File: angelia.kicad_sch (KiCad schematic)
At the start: 428 parts, among them J10 Conn_Coaxial, J15 Conn_02x05_Top_Bottom, J16 Conn_02x13_Top_Bottom, J18 Conn_02x05_Top_Bottom, J25 Conn_Coaxial, J3 Conn_Coaxial, J33 ATX-20, J5 Conn_Coaxial, J7 RJ45, P1 Conn_02x05_Top_Bottom, P2 Conn_02x05_Top_Bottom, P3 EP4CE115F780, U10 LTC2208xUP, U11 LTC6400, U13 KSZ9021RL, U14 SN65LVDM180D, U18 LTC2208xUP, U19 TO-252-5, U2 TLV320AIC23BPW, U20 74LCX541MTC, U22 ULN2003A, U23 LTC6400, U25 74LCX541MTC, U27 TO-252-3, U3 LMC6482AM, U31 TO-252-5, U4 LMC6482AM, U5 AD9744, U6 OPA2674IC, U7 OPA2674IC

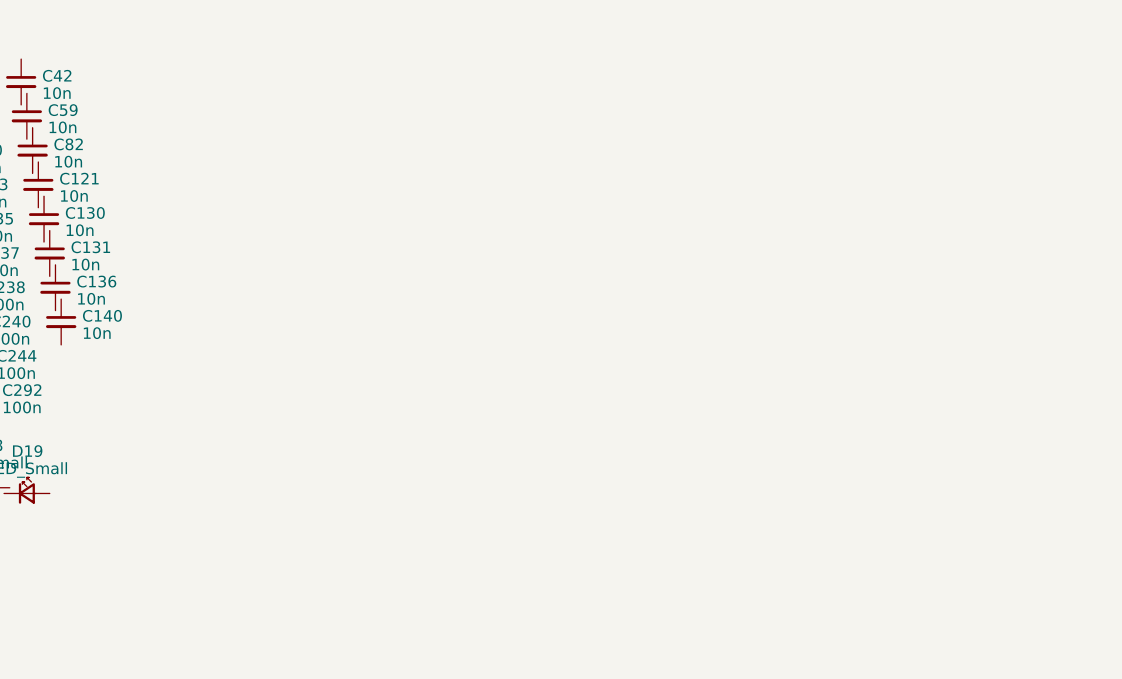
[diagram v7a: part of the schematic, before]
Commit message: botom side completed
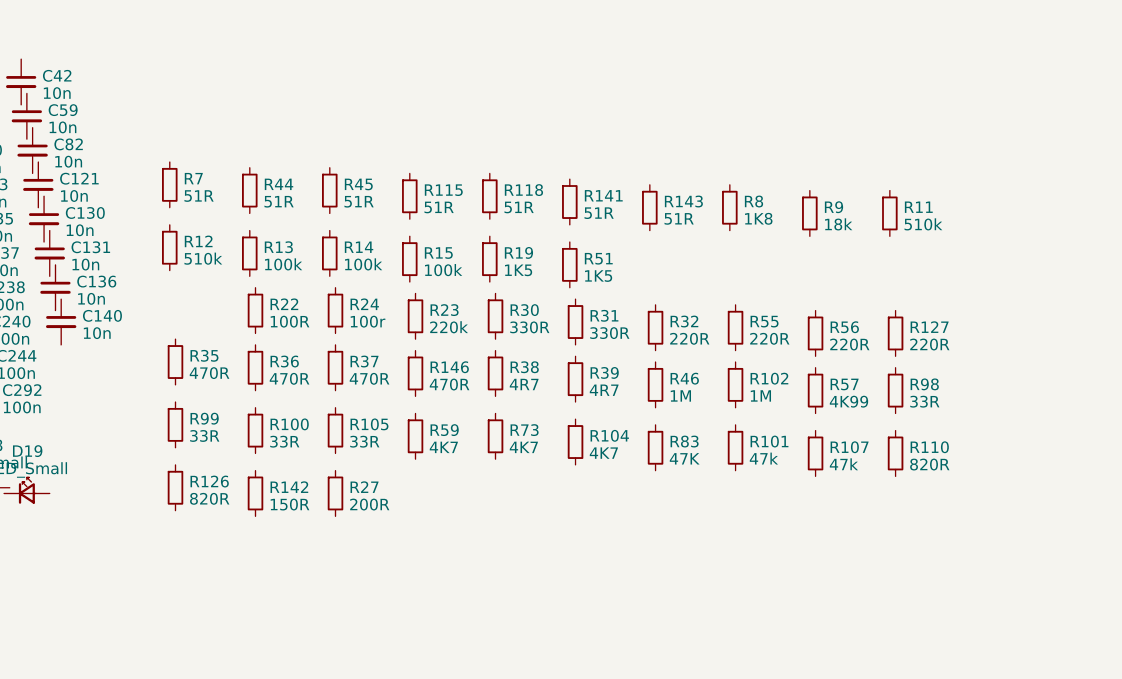
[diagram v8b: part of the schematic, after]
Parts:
- added R100, R105, R98, R99: 33R, Resistor_SMD:R_0805_2012Metric, symbol Device:R_Small
- added R101, R107: 47k, Resistor_SMD:R_0805_2012Metric, symbol Device:R_Small
- added R102, R46: 1M, Resistor_SMD:R_0805_2012Metric, symbol Device:R_Small
- added R104, R59, R73: 4K7, Resistor_SMD:R_0805_2012Metric, symbol Device:R_Small
- added R11, R12: 510k, Resistor_SMD:R_0805_2012Metric, symbol Device:R_Small
- added R110, R126: 820R, Resistor_SMD:R_0805_2012Metric, symbol Device:R_Small
- added R115, R118, R141, R143, R44, R45, R7: 51R, Resistor_SMD:R_0805_2012Metric, symbol Device:R_Small
- added R127, R32, R55, R56: 220R, Resistor_SMD:R_0805_2012Metric, symbol Device:R_Small
- added R13, R14, R15: 100k, Resistor_SMD:R_0805_2012Metric, symbol Device:R_Small
- added R142: 150R, Resistor_SMD:R_0805_2012Metric, symbol Device:R_Small
- added R146, R35, R36, R37: 470R, Resistor_SMD:R_0805_2012Metric, symbol Device:R_Small
- added R19, R51: 1K5, Resistor_SMD:R_0805_2012Metric, symbol Device:R_Small
- added R22: 100R, Resistor_SMD:R_0805_2012Metric, symbol Device:R_Small
- added R23: 220k, Resistor_SMD:R_0805_2012Metric, symbol Device:R_Small
- added R24: 100r, Resistor_SMD:R_0805_2012Metric, symbol Device:R_Small
- added R27: 200R, Resistor_SMD:R_0805_2012Metric, symbol Device:R_Small
- added R30, R31: 330R, Resistor_SMD:R_0805_2012Metric, symbol Device:R_Small
- added R38, R39: 4R7, Resistor_SMD:R_0805_2012Metric, symbol Device:R_Small
- added R57: 4K99, Resistor_SMD:R_0805_2012Metric, symbol Device:R_Small
- added R8: 1K8, Resistor_SMD:R_0805_2012Metric, symbol Device:R_Small
- added R83: 47K, Resistor_SMD:R_0805_2012Metric, symbol Device:R_Small
- added R9: 18k, Resistor_SMD:R_0805_2012Metric, symbol Device:R_Small
